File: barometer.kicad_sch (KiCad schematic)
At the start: 0 parts

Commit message: Initial component symbol placement
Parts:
- added U15: BM1390GLV-ZTR, Library:LGA-10_L2.0-W2.0-P0.50-BL, symbol Library:BM1390GLV-ZTR
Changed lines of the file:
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@@
 	(generator_version "9.0")
 	(paper "A4")
+	(symbol
+		(lib_id "Library:BM1390GLV-ZTR")
+		(at 153.67 99.06 0)
+		(unit 1)
+		(exclude_from_sim no)
+		(in_bom yes)
+		(on_board yes)
+		(dnp no)
+		(fields_autoplaced yes)
+		(property "Reference" "U15"
+			(at 153.67 86.36 0)
+			(effects
+				(font
+					(size 1.27 1.27)
+				)
+			)
+		)
+		(property "Value" "BM1390GLV-ZTR"
+			(at 153.67 88.9 0)
+			(effects
+				(font
+					(size 1.27 1.27)
+				)
+			)
+		)
+		(property "Footprint" "Library:LGA-10_L2.0-W2.0-P0.50-BL"
+			(at 153.67 111.76 0)
+			(effects
+				(font
+					(size 1.27 1.27)
+				)
+				(hide yes)
+			)
+		)
+		(property "Datasheet" "https://www.lcsc.com/datasheet/C3252182.pdf"
+			(at 153.67 114.3 0)
+			(effects
+				(font
+					(size 1.27 1.27)
+				)
+				(hide yes)
+			)
+		)
+		(property "Description" ""
+			(at 153.67 99.06 0)
+			(effects
+				(font
+					(size 1.27 1.27)
+				)
+				(hide yes)
+			)
+		)
+		(property "Manufacturer" "ROHM(罗姆)"
+			(at 153.67 116.84 0)
+			(effects
+				(font
+					(size 1.27 1.27)
+				)
+				(hide yes)
+			)
+		)
+		(property "MPN" "BM1390GLV-ZTR"
+			(at 153.67 119.38 0)
+			(effects
+				(font
+					(size 1.27 1.27)
+				)
+				(hide yes)
+			)
+		)
+		(property "LCSC Part" "C3252182"
+			(at 153.67 121.92 0)
+			(effects
+				(font
+					(size 1.27 1.27)
+				)
+				(hide yes)
+			)
+		)
+		(pin "3"
+		)
+		(pin "2"
+		)
+		(pin "8"
+		)
+		(pin "4"
+		)
+		(pin "10"
+		)
+		(pin "7"
+		)
+		(pin "5"
+		)
+		(pin "9"
+		)
+		(pin "6"
+		)
+		(pin "1"
+		)
+		(instances
+			(project ""
+				(path "/6af311bf-2fb1-446c-8c7e-7c930a463809/fa094b53-b74b-46c1-9025-be834bb944fa"
+					(reference "U15")
+					(unit 1)
+				)
+			)
+		)
+	)
 )

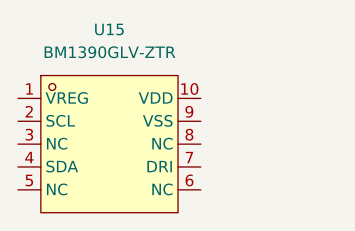
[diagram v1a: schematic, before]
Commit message: Barometer & ToF Hierarchical Schematic Updates
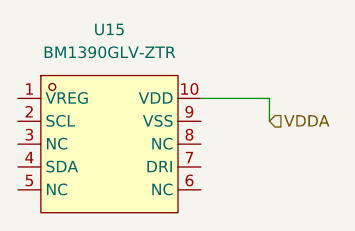
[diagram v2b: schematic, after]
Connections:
- net VDDA: now reaches U15.10 (VDD)
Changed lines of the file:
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@@
 	(generator_version "9.0")
 	(paper "A4")
+	(wire
+		(pts
+			(xy 171.45 96.52) (xy 171.45 93.98)
+		)
+		(stroke
+			(width 0)
+			(type default)
+		)
+	)
+	(wire
+		(pts
+			(xy 163.83 93.98) (xy 171.45 93.98)
+		)
+		(stroke
+			(width 0)
+			(type default)
+		)
+	)
+	(hierarchical_label "VDDA"
+		(shape input)
+		(at 171.45 96.52 0)
+		(effects
+			(font
+				(size 1.27 1.27)
+			)
+			(justify left)
+		)
+	)
 	(symbol
 		(lib_id "Library:BM1390GLV-ZTR")

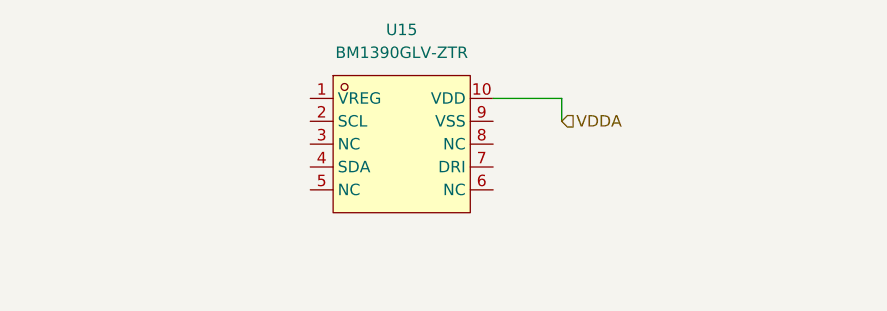
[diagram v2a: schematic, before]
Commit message: MCU implementation start Still needs component schematic checks & component integration with MCU
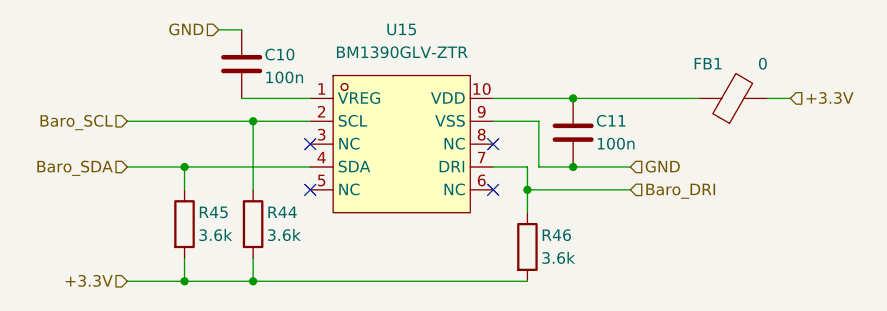
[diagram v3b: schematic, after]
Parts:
- added C10, C11: 100n, symbol Device:C
- added FB1: 0, symbol Device:FerriteBead
- added R44, R45, R46: 3.6k, symbol Device:R
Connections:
- net at U15.1 (VREG): now also C10.2
- net Baro_SCL: now reaches U15.2 (SCL)
- net Baro_SCL: now also R44.1
- net Baro_SDA: now reaches U15.4 (SDA)
- net Baro_SDA: now also R45.1
- net Baro_DRI: now reaches U15.7 (DRI)
- net Baro_DRI: now also R46.1
- net GND: now reaches U15.9 (VSS)
- net GND: now also C10.1, C11.2
- net VDDA: no longer names the net of U15.10 (VDD)
- net VDDA: now also C11.1, FB1.1
- new net +3.3V: FB1.2, R44.2, R45.2, R46.2
- no-connect marks 0 -> 4

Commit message: MCU Integration & Sensor Ports
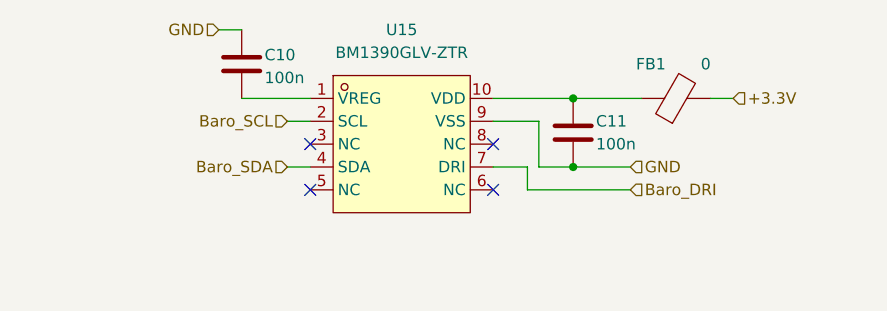
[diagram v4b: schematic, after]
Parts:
- removed R44, R45, R46: 3.6k, symbol Device:R
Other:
- moved on the sheet: FB1
